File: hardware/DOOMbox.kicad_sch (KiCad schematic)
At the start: 36 parts, among them J1 DE15_Socket_HighDensity, J2 AudioJack3, SW1 SW_SPST, SW2 SW_Push, U1 RPi Pico 2, U3 AP7381-50SA-7, U4 LM324N, U5 CD4010BE

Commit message: Stripboard layout WIP + custom footprints
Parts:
- BZ1: footprint (none) -> Buzzer_Beeper:Indicator_PUI_AI-1440-TWT-24V-2-R
- C1, C10, C2, C8: footprint (none) -> Capacitor_THT:C_Rect_L7.0mm_W2.0mm_P5.00mm
- C12, C4: footprint (none) -> Capacitor_THT:CP_Radial_D5.0mm_P2.50mm
- C3, C5: footprint (none) -> Capacitor_THT:CP_Radial_Tantal_D4.5mm_P2.50mm
- D1: footprint (none) -> Diode_THT:D_5W_P12.70mm_Horizontal
- D2, J1, J2, SW1, SW2: footprint (none) -> Stripboard:Peripheral_Offboard
- R1, R10, R12, R13, R15, R16, R17, R2, R3, R4, R5, R6, R7, R8, R9: footprint (none) -> Resistor_THT:R_Axial_DIN0309_L9.0mm_D3.2mm_P12.70mm_Horizontal
- RV1, RV2: footprint (none) -> Potentiometer_THT:Potentiometer_Vishay_T73YP_Vertical
- U3: footprint Package_TO_SOT_SMD:SOT-23 -> Package_TO_SOT_THT:TO-92_Inline_Wide
- U4: footprint (none) -> Package_DIP:DIP-14_W7.62mm
- U5: footprint (none) -> Package_DIP:DIP-16_W7.62mm
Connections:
- net at U1.21 (GPIO16): no longer BZ1.1 (+)
- net at U1.25 (GPIO19): now also BZ1.1 (+)
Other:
- moved on the sheet: BZ1
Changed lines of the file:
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@@
 	)
 	(junction
-		(at 100.33 144.78)
-		(diameter 0)
-		(color 0 0 0 0)
-	)
-	(junction
 		(at 57.15 109.22)
 		(diameter 0)
@@
 	(wire
 		(pts
-			(xy 97.79 139.7) (xy 104.14 139.7)
-		)
-		(stroke
-			(width 0)
-			(type default)
-		)
-	)
-	(wire
-		(pts
 			(xy 161.29 182.88) (xy 158.75 182.88)
 		)
@@
 	(wire
 		(pts
-			(xy 180.34 137.16) (xy 182.88 137.16)
+			(xy 100.33 134.62) (xy 101.6 134.62)
 		)
 		(stroke
@@
 	(wire
 		(pts
-			(xy 100.33 144.78) (xy 104.14 144.78)
+			(xy 180.34 137.16) (xy 182.88 137.16)
 		)
 		(stroke
@@
 	(wire
 		(pts
-			(xy 100.33 134.62) (xy 100.33 144.78)
+			(xy 100.33 134.62) (xy 100.33 147.32)
 		)
 		(stroke
@@
 	(wire
 		(pts
-			(xy 100.33 144.78) (xy 100.33 147.32)
+			(xy 210.82 138.43) (xy 213.36 138.43)
 		)
 		(stroke
@@
 	(wire
 		(pts
-			(xy 210.82 138.43) (xy 213.36 138.43)
+			(xy 55.88 127) (xy 59.69 127)
 		)
 		(stroke
@@
 	(wire
 		(pts
-			(xy 55.88 127) (xy 59.69 127)
+			(xy 161.29 172.72) (xy 161.29 173.99)
 		)
 		(stroke
@@
 	(wire
 		(pts
-			(xy 161.29 172.72) (xy 161.29 173.99)
+			(xy 97.79 129.54) (xy 101.6 129.54)
 		)
 		(stroke
@@
 			)
 		)
-		(property "Footprint" ""
+		(property "Footprint" "Package_DIP:DIP-14_W7.62mm"
 			(at 210.82 44.45 0)
 			(effects
@@
 			)
 		)
-		(property "Footprint" ""
+		(property "Footprint" "Capacitor_THT:C_Rect_L7.0mm_W2.0mm_P5.00mm"
 			(at 117.1448 41.91 0)
 			(effects
@@
 			)
 		)
-		(property "Footprint" ""
+		(property "Footprint" "Package_DIP:DIP-14_W7.62mm"
 			(at 261.62 29.21 0)
 			(effects
@@
 			)
 		)
-		(property "Footprint" ""
+		(property "Footprint" "Capacitor_THT:CP_Radial_Tantal_D4.5mm_P2.50mm"
 			(at 121.6152 181.61 0)
 			(effects
@@
 			)
 		)
-		(property "Footprint" ""
+		(property "Footprint" "Potentiometer_THT:Potentiometer_Vishay_T73YP_Vertical"
 			(at 191.77 73.66 0)
 			(effects
@@
 			)
 		)
-		(property "Footprint" ""
+		(property "Footprint" "Package_DIP:DIP-14_W7.62mm"
 			(at 179.07 71.12 0)
 			(effects
@@
 		(on_board yes)
 		(dnp no)
-		(fields_autoplaced yes)
 		(property "Reference" "U3"
 			(at 133.35 166.37 0)
@@
 			)
 		)
-		(property "Footprint" "Package_TO_SOT_SMD:SOT-23"
-			(at 133.35 182.88 0)
+		(property "Footprint" "Package_TO_SOT_THT:TO-92_Inline_Wide"
+			(at 138.684 164.592 0)
 			(effects
 				(font
@@
 			)
 		)
-		(property "Footprint" ""
+		(property "Footprint" "Stripboard:Peripheral_Offboard"
 			(at 106.68 111.76 0)
 			(effects
@@
 			)
 		)
-		(property "Footprint" ""
+		(property "Footprint" "Resistor_THT:R_Axial_DIN0309_L9.0mm_D3.2mm_P12.70mm_Horizontal"
 			(at 238.76 43.688 90)
 			(effects
@@
 			)
 		)
-		(property "Footprint" ""
+		(property "Footprint" "Capacitor_THT:C_Rect_L7.0mm_W2.0mm_P5.00mm"
 			(at 167.3352 53.34 0)
 			(effects
@@
 			)
 		)
-		(property "Footprint" ""
+		(property "Footprint" "Resistor_THT:R_Axial_DIN0309_L9.0mm_D3.2mm_P12.70mm_Horizontal"
 			(at 176.53 107.442 90)
 			(effects
@@
 			)
 		)
-		(property "Footprint" ""
+		(property "Footprint" "Stripboard:Peripheral_Offboard"
 			(at 161.29 177.8 0)
 			(effects
@@
 			)
 		)
-		(property "Footprint" ""
+		(property "Footprint" "Capacitor_THT:C_Rect_L7.0mm_W2.0mm_P5.00mm"
 			(at 167.3352 80.01 0)
 			(effects
@@
 			)
 		)
-		(property "Footprint" ""
+		(property "Footprint" "Resistor_THT:R_Axial_DIN0309_L9.0mm_D3.2mm_P12.70mm_Horizontal"
 			(at 176.53 112.522 90)
 			(effects
@@
 			)
 		)
-		(property "Footprint" ""
+		(property "Footprint" "Diode_THT:D_5W_P12.70mm_Horizontal"
 			(at 104.14 93.98 0)
 			(effects
@@
 			)
 		)
-		(property "Footprint" ""
+		(property "Footprint" "Resistor_THT:R_Axial_DIN0309_L9.0mm_D3.2mm_P12.70mm_Horizontal"
 			(at 233.68 127.508 90)
 			(effects
@@
 			)
 		)
-		(property "Footprint" ""
+		(property "Footprint" "Resistor_THT:R_Axial_DIN0309_L9.0mm_D3.2mm_P12.70mm_Horizontal"
 			(at 176.53 117.602 90)
 			(effects
@@
 			)
 		)
-		(property "Footprint" ""
+		(property "Footprint" "Resistor_THT:R_Axial_DIN0309_L9.0mm_D3.2mm_P12.70mm_Horizontal"
 			(at 154.94 184.658 90)
 			(effects
@@
 			)
 		)
-		(property "Footprint" ""
+		(property "Footprint" "Package_DIP:DIP-16_W7.62mm"
 			(at 130.81 58.42 0)
 			(effects
@@
 			)
 		)
-		(property "Footprint" ""
+		(property "Footprint" "Resistor_THT:R_Axial_DIN0309_L9.0mm_D3.2mm_P12.70mm_Horizontal"
 			(at 176.53 148.082 90)
 			(effects
@@
 			)
 		)
-		(property "Footprint" ""
+		(property "Footprint" "Package_DIP:DIP-14_W7.62mm"
 			(at 210.82 71.12 0)
 			(effects
@@
 			)
 		)
-		(property "Footprint" ""
+		(property "Footprint" "Capacitor_THT:CP_Radial_D5.0mm_P2.50mm"
 			(at 233.68 67.6148 0)
 			(effects
@@
 			)
 		)
-		(property "Footprint" ""
+		(property "Footprint" "Capacitor_THT:CP_Radial_Tantal_D4.5mm_P2.50mm"
 			(at 147.0152 181.61 0)
 			(effects
@@
 			)
 		)
-		(property "Footprint" ""
+		(property "Footprint" "Resistor_THT:R_Axial_DIN0309_L9.0mm_D3.2mm_P12.70mm_Horizontal"
 			(at 160.02 46.228 90)
 			(effects
@@
 			)
 		)
-		(property "Footprint" ""
+		(property "Footprint" "Stripboard:Peripheral_Offboard"
 			(at 114.3 172.72 0)
 			(effects
@@
 			)
 		)
-		(property "Footprint" ""
+		(property "Footprint" "Stripboard:Peripheral_Offboard"
 			(at 196.85 135.89 0)
 			(effects
@@
 			)
 		)
-		(property "Footprint" ""
+		(property "Footprint" "Capacitor_THT:CP_Radial_D5.0mm_P2.50mm"
 			(at 233.68 40.9448 0)
 			(effects
@@
 			)
 		)
-		(property "Footprint" ""
+		(property "Footprint" "Resistor_THT:R_Axial_DIN0309_L9.0mm_D3.2mm_P12.70mm_Horizontal"
 			(at 233.68 122.428 90)
 			(effects
@@
 			)
 		)
-		(property "Footprint" ""
+		(property "Footprint" "Resistor_THT:R_Axial_DIN0309_L9.0mm_D3.2mm_P12.70mm_Horizontal"
 			(at 176.53 130.302 90)
 			(effects
@@
 			)
 		)
-		(property "Footprint" ""
+		(property "Footprint" "Capacitor_THT:C_Rect_L7.0mm_W2.0mm_P5.00mm"
 			(at 268.9352 38.1 0)
 			(effects
@@
 	(symbol
 		(lib_id "Device:Buzzer")
-		(at 106.68 142.24 0)
+		(at 104.14 132.08 0)
 		(unit 1)
 		(exclude_from_sim no)
@@
 		(on_board yes)
 		(dnp no)
-		(fields_autoplaced yes)
 		(property "Reference" "BZ1"
-			(at 110.49 140.9699 0)
+			(at 107.95 130.8099 0)
 			(effects
 				(font
@@
 		)
 		(property "Value" "Buzzer"
-			(at 110.49 143.5099 0)
+			(at 107.95 133.3499 0)
 			(effects
 				(font
@@
 			)
 		)
-		(property "Footprint" ""
-			(at 106.045 139.7 90)
+		(property "Footprint" "Buzzer_Beeper:Indicator_PUI_AI-1440-TWT-24V-2-R"
+			(at 103.505 129.54 90)
 			(effects
 				(font
@@
 		)
 		(property "Datasheet" "~"
-			(at 106.045 139.7 90)
+			(at 103.505 129.54 90)
 			(effects
 				(font
@@
 		)
 		(property "Description" "Buzzer, polarized"
-			(at 106.68 142.24 0)
+			(at 104.14 132.08 0)
 			(effects
 				(font
@@
 			)
 		)
-		(property "Footprint" ""
+		(property "Footprint" "Resistor_THT:R_Axial_DIN0309_L9.0mm_D3.2mm_P12.70mm_Horizontal"
 			(at 160.02 72.898 90)
 			(effects
@@
 			)
 		)
-		(property "Footprint" ""
+		(property "Footprint" "Resistor_THT:R_Axial_DIN0309_L9.0mm_D3.2mm_P12.70mm_Horizontal"
 			(at 176.53 143.002 90)
 			(effects
@@
 			)
 		)
-		(property "Footprint" ""
+		(property "Footprint" "Stripboard:Peripheral_Offboard"
 			(at 257.81 55.88 0)
 			(effects
@@
 			)
 		)
-		(property "Footprint" ""
+		(property "Footprint" "Resistor_THT:R_Axial_DIN0309_L9.0mm_D3.2mm_P12.70mm_Horizontal"
 			(at 176.53 135.382 90)
 			(effects
@@
 			)
 		)
-		(property "Footprint" ""
+		(property "Footprint" "Potentiometer_THT:Potentiometer_Vishay_T73YP_Vertical"
 			(at 191.77 46.99 0)
 			(effects
@@
 			)
 		)
-		(property "Footprint" ""
+		(property "Footprint" "Resistor_THT:R_Axial_DIN0309_L9.0mm_D3.2mm_P12.70mm_Horizontal"
 			(at 238.76 70.358 90)
 			(effects
@@
 			)
 		)
-		(property "Footprint" ""
+		(property "Footprint" "Resistor_THT:R_Axial_DIN0309_L9.0mm_D3.2mm_P12.70mm_Horizontal"
 			(at 176.53 125.222 90)
 			(effects
@@
 			)
 		)
-		(property "Footprint" ""
+		(property "Footprint" "Package_DIP:DIP-14_W7.62mm"
 			(at 179.07 44.45 0)
 			(effects

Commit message: Complete stripboard design
Squashed commit of the following:

commit dbad1e7bdfb2dba54c7140f3a2191c6905e5781a
Author: Jack Bennett <jackbennett0708@gmail.com>
Date:   Sat Aug 30 16:36:03 2025 +0100

    Complete

commit 05059f46a42e6744a15d06e69ba94dfb8af3ae9c
Author: Jack Bennett <jackbennett0708@gmail.com>
Date:   Sat Aug 30 14:41:32 2025 +0100

    1
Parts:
- D1: footprint Diode_THT:D_5W_P12.70mm_Horizontal -> Diode_THT:D_A-405_P7.62mm_Horizontal
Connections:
- net at U1.25 (GPIO19): no longer BZ1.1 (+)
- net at U1.26 (GPIO20): now also BZ1.1 (+)
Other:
- moved on the sheet: BZ1
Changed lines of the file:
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@@
 	(wire
 		(pts
-			(xy 191.77 41.91) (xy 191.77 43.18)
+			(xy 97.79 127) (xy 102.87 127)
 		)
 		(stroke
@@
 	(wire
 		(pts
-			(xy 100.33 134.62) (xy 101.6 134.62)
+			(xy 191.77 41.91) (xy 191.77 43.18)
 		)
 		(stroke
@@
 	(wire
 		(pts
+			(xy 102.87 132.08) (xy 102.87 134.62)
+		)
+		(stroke
+			(width 0)
+			(type default)
+		)
+	)
+	(wire
+		(pts
 			(xy 203.2 66.04) (xy 204.47 66.04)
 		)
@@
 	(wire
 		(pts
-			(xy 203.2 35.56) (xy 220.98 35.56)
+			(xy 102.87 134.62) (xy 100.33 134.62)
 		)
 		(stroke
@@
 	(wire
 		(pts
-			(xy 55.88 114.3) (xy 59.69 114.3)
+			(xy 203.2 35.56) (xy 220.98 35.56)
 		)
 		(stroke
@@
 	(wire
 		(pts
-			(xy 226.06 41.91) (xy 220.98 41.91)
+			(xy 55.88 114.3) (xy 59.69 114.3)
 		)
 		(stroke
@@
 	(wire
 		(pts
-			(xy 210.82 138.43) (xy 213.36 138.43)
+			(xy 226.06 41.91) (xy 220.98 41.91)
 		)
 		(stroke
@@
 	(wire
 		(pts
-			(xy 55.88 127) (xy 59.69 127)
+			(xy 210.82 138.43) (xy 213.36 138.43)
 		)
 		(stroke
@@
 	(wire
 		(pts
-			(xy 161.29 172.72) (xy 161.29 173.99)
+			(xy 55.88 127) (xy 59.69 127)
 		)
 		(stroke
@@
 	(wire
 		(pts
-			(xy 97.79 129.54) (xy 101.6 129.54)
+			(xy 161.29 172.72) (xy 161.29 173.99)
 		)
 		(stroke
@@
 			)
 		)
-		(property "Footprint" "Diode_THT:D_5W_P12.70mm_Horizontal"
+		(property "Footprint" "Diode_THT:D_A-405_P7.62mm_Horizontal"
 			(at 104.14 93.98 0)
 			(effects
@@
 	(symbol
 		(lib_id "Device:Buzzer")
-		(at 104.14 132.08 0)
+		(at 105.41 129.54 0)
 		(unit 1)
 		(exclude_from_sim no)
@@
 		(dnp no)
 		(property "Reference" "BZ1"
-			(at 107.95 130.8099 0)
+			(at 109.22 128.2699 0)
 			(effects
 				(font
@@
 		)
 		(property "Value" "Buzzer"
-			(at 107.95 133.3499 0)
+			(at 109.22 130.8099 0)
 			(effects
 				(font
@@
 		)
 		(property "Footprint" "Buzzer_Beeper:Indicator_PUI_AI-1440-TWT-24V-2-R"
-			(at 103.505 129.54 90)
+			(at 104.775 127 90)
 			(effects
 				(font
@@
 		)
 		(property "Datasheet" "~"
-			(at 103.505 129.54 90)
+			(at 104.775 127 90)
 			(effects
 				(font
@@
 		)
 		(property "Description" "Buzzer, polarized"
-			(at 104.14 132.08 0)
+			(at 105.41 129.54 0)
 			(effects
 				(font

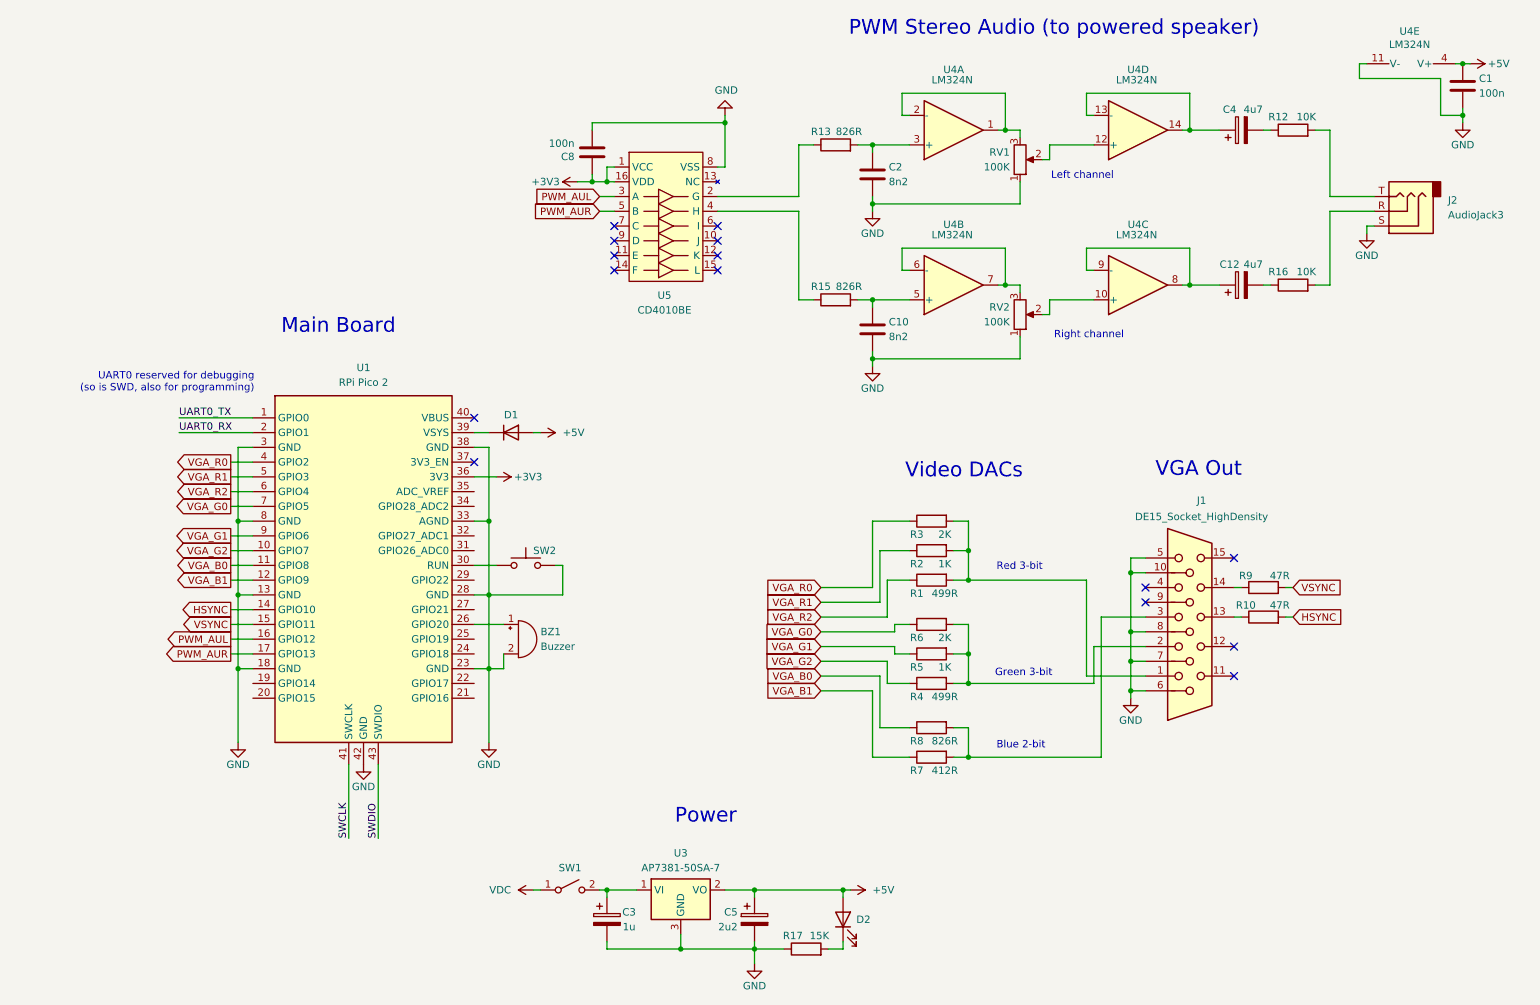
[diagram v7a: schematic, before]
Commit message: Rework stripboard design (+ edit sb symbols)
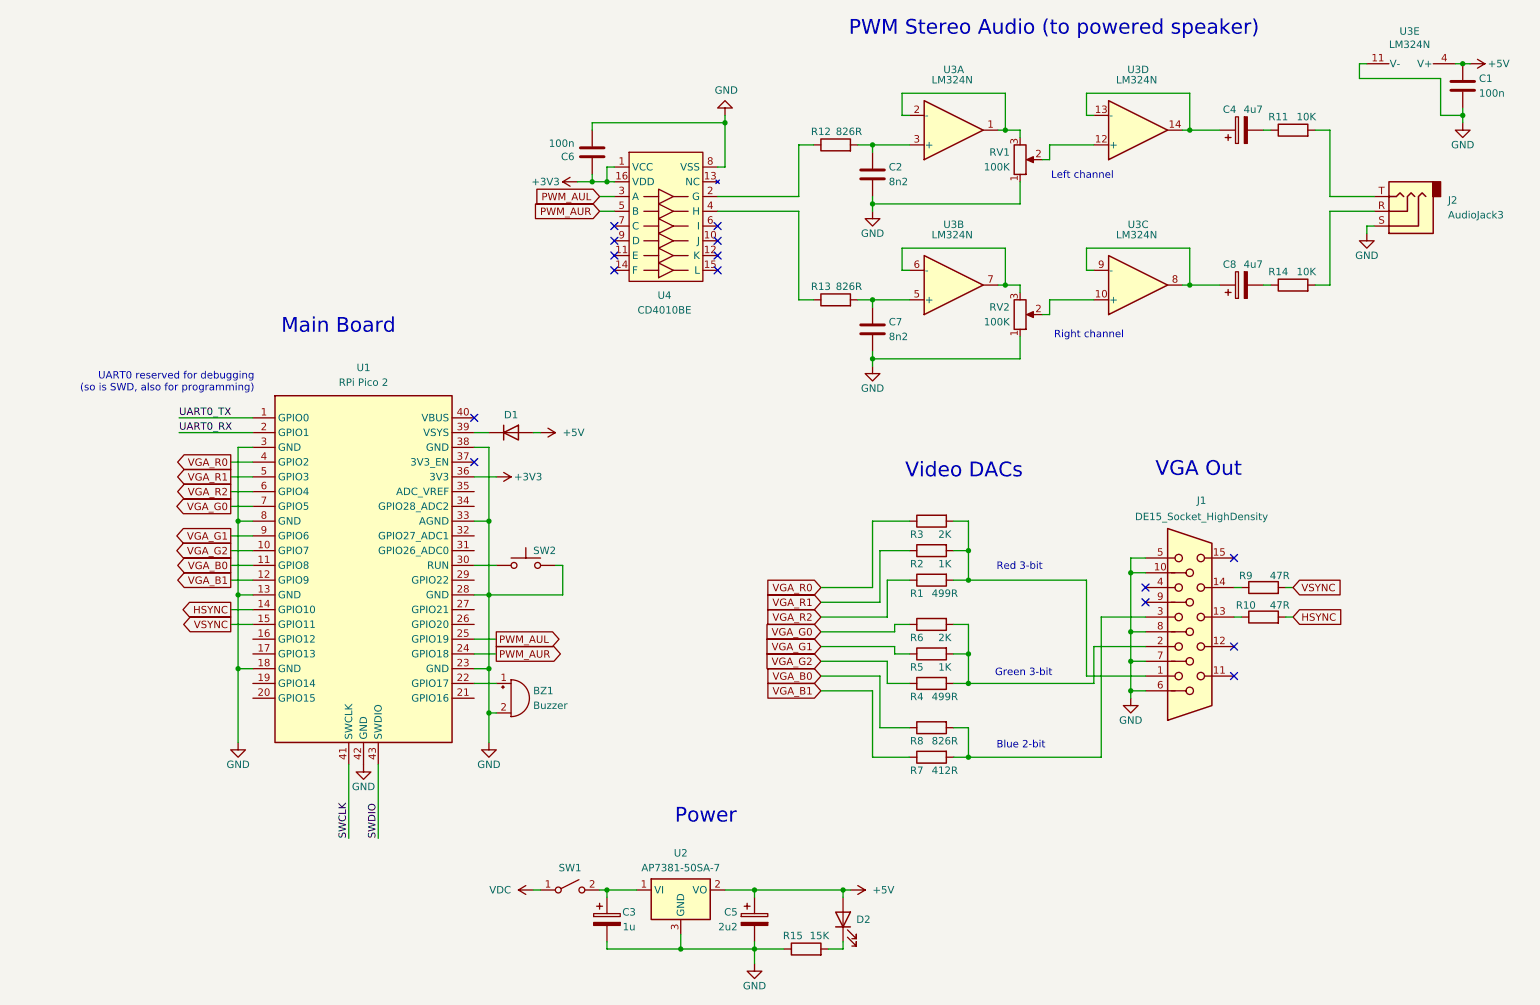
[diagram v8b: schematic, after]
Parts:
- C3, C5: footprint Capacitor_THT:CP_Radial_Tantal_D4.5mm_P2.50mm -> Capacitor_THT:C_Disc_D3.0mm_W1.6mm_P2.50mm
- R1, R10, R2, R3, R4, R5, R6, R7, R8, R9: footprint Resistor_THT:R_Axial_DIN0309_L9.0mm_D3.2mm_P12.70mm_Horizontal -> Resistor_THT:R_Axial_DIN0207_L6.3mm_D2.5mm_P10.16mm_Horizontal
- R11: renamed from R12; footprint Resistor_THT:R_Axial_DIN0309_L9.0mm_D3.2mm_P12.70mm_Horizontal -> Resistor_THT:R_Axial_DIN0207_L6.3mm_D2.5mm_P7.62mm_Horizontal
- R14: renamed from R16; footprint Resistor_THT:R_Axial_DIN0309_L9.0mm_D3.2mm_P12.70mm_Horizontal -> Resistor_THT:R_Axial_DIN0207_L6.3mm_D2.5mm_P7.62mm_Horizontal
- R15: renamed from R17; footprint Resistor_THT:R_Axial_DIN0309_L9.0mm_D3.2mm_P12.70mm_Horizontal -> Resistor_THT:R_Axial_DIN0309_L9.0mm_D3.2mm_P5.08mm_Vertical
- renumbered C8 to C6, C10 to C7, C12 to C8, R13 to R12, R15 to R13, U3 to U2, U4 to U3, U5 to U4
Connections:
- net PWM_AUL: now also U1.25 (GPIO19); no longer U1.16 (GPIO12)
- net PWM_AUR: now also U1.24 (GPIO18); no longer U1.17 (GPIO13)
- net at U1.22 (GPIO17): now also BZ1.1 (+)
- net at U1.26 (GPIO20): no longer BZ1.1 (+)
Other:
- moved on the sheet: BZ1
